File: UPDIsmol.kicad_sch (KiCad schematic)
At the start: 38 parts, among them J1 USB_C_Receptacle_USB2.0, J2 Conn_01x03, Q1 SI2301, SW1 12V UPDI, U1 CH340G, U2 LTC1262, U4 74AHCT1G125, Y1 445C25D12M00000

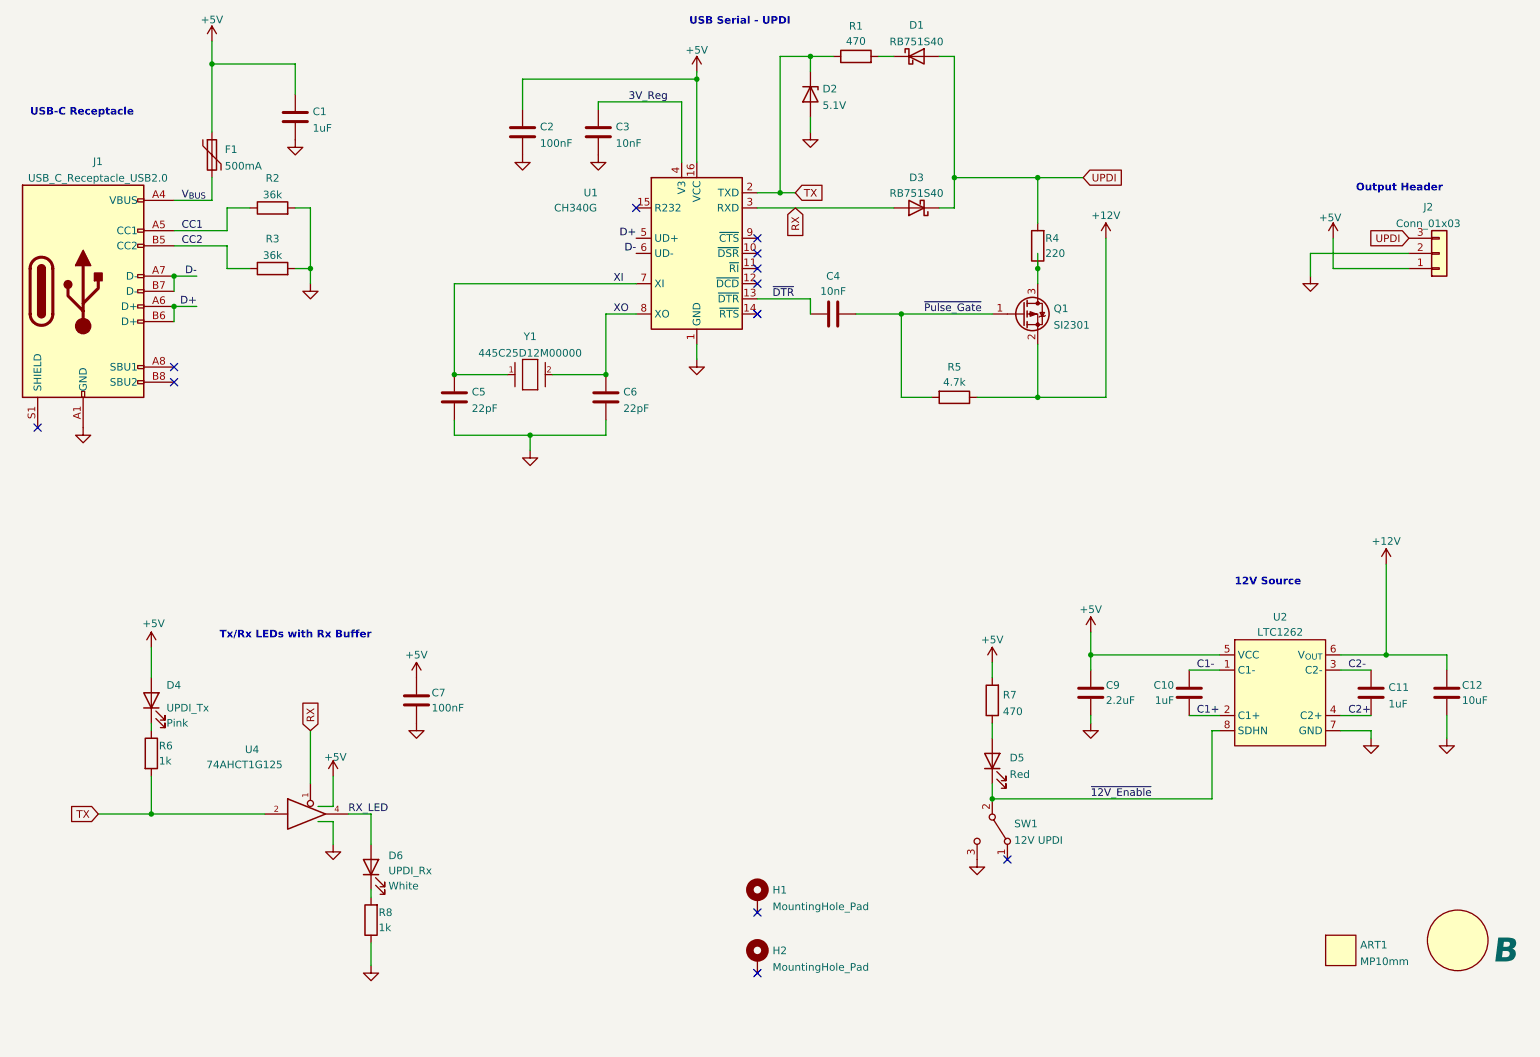
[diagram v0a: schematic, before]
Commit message: Tidied schematic, still RevB
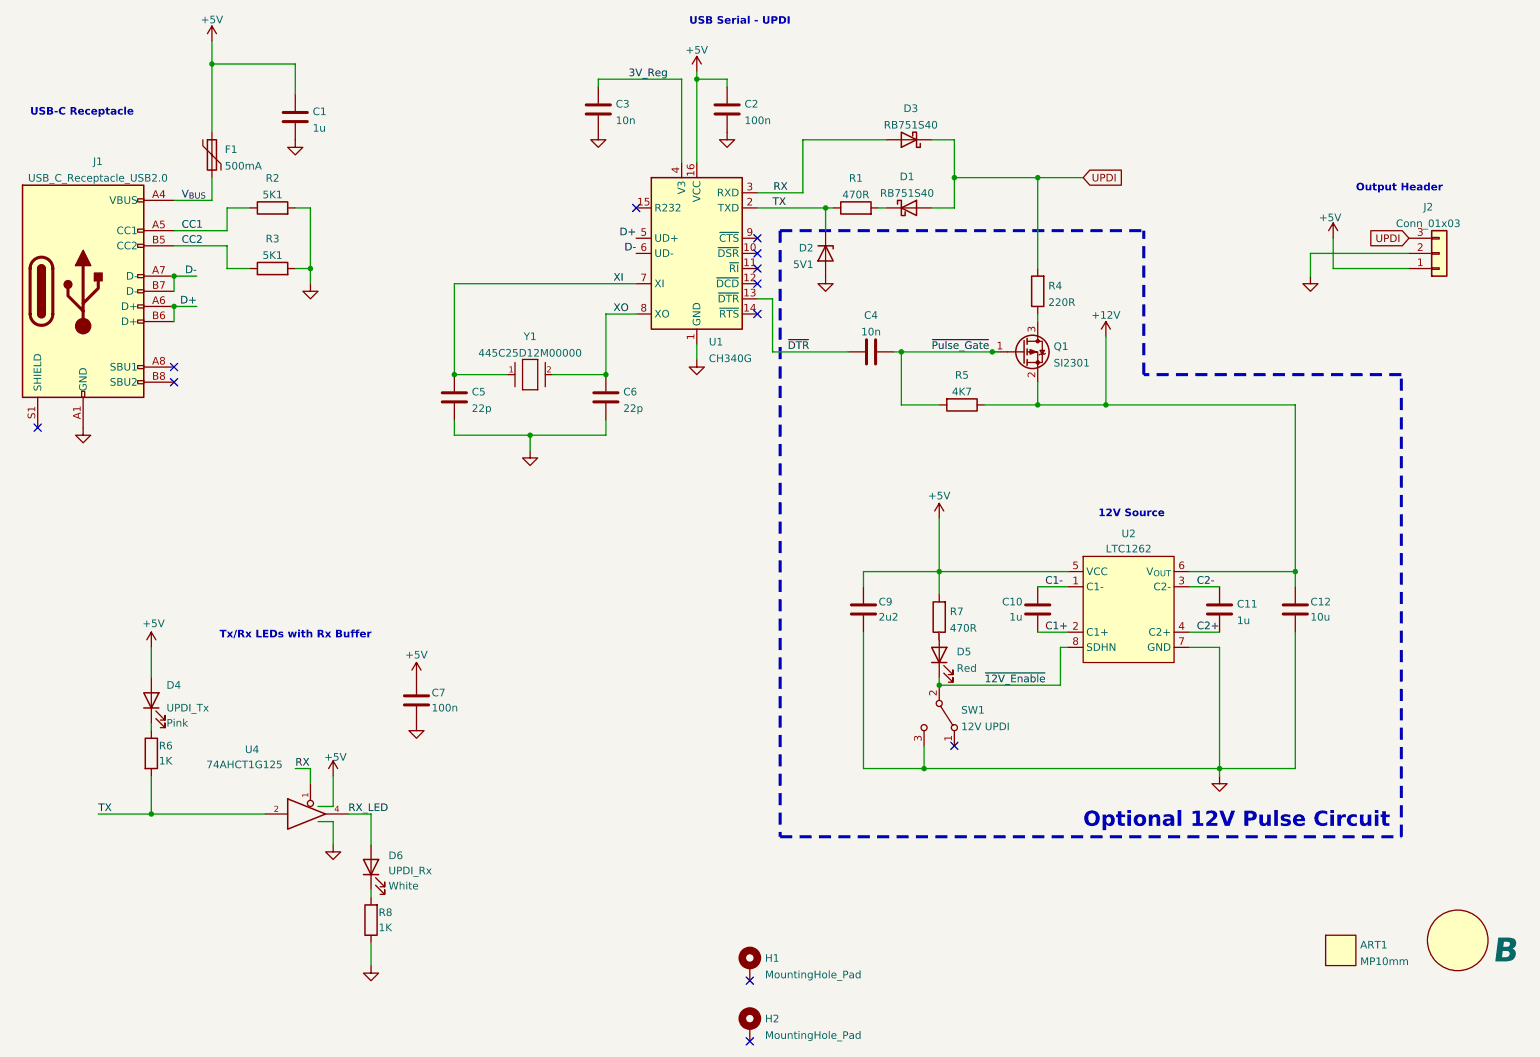
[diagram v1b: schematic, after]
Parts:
- C1, C10, C11: value 1uF -> 1u
- C12: value 10uF -> 10u
- C2, C7: value 100nF -> 100n
- C3, C4: value 10nF -> 10n
- C5, C6: value 22pF -> 22p
- C9: value 2.2uF -> 2u2
- D2: value 5.1V -> 5V1
- R1, R7: value 470 -> 470R
- R2, R3: value 36k -> 5K1
- R4: value 220 -> 220R
- R5: value 4.7k -> 4K7
- R6, R8: value 1k -> 1K
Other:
- note added: "Optional 12V Pulse Circuit"
- moved on the sheet: C10, C11, C12, C2, C3, C4, C9, D1, D2, D3, D5, H1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
